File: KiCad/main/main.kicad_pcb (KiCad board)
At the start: 4 copper layers, 160 x 100.1 mm, 35 parts, among them SW1 SW_Push, U1 74HC245, U10 8254, U11 8259, U12 27C512, U2 8284, U3 74HC245, U4 8086, U5 74HC573, U6 74HC573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

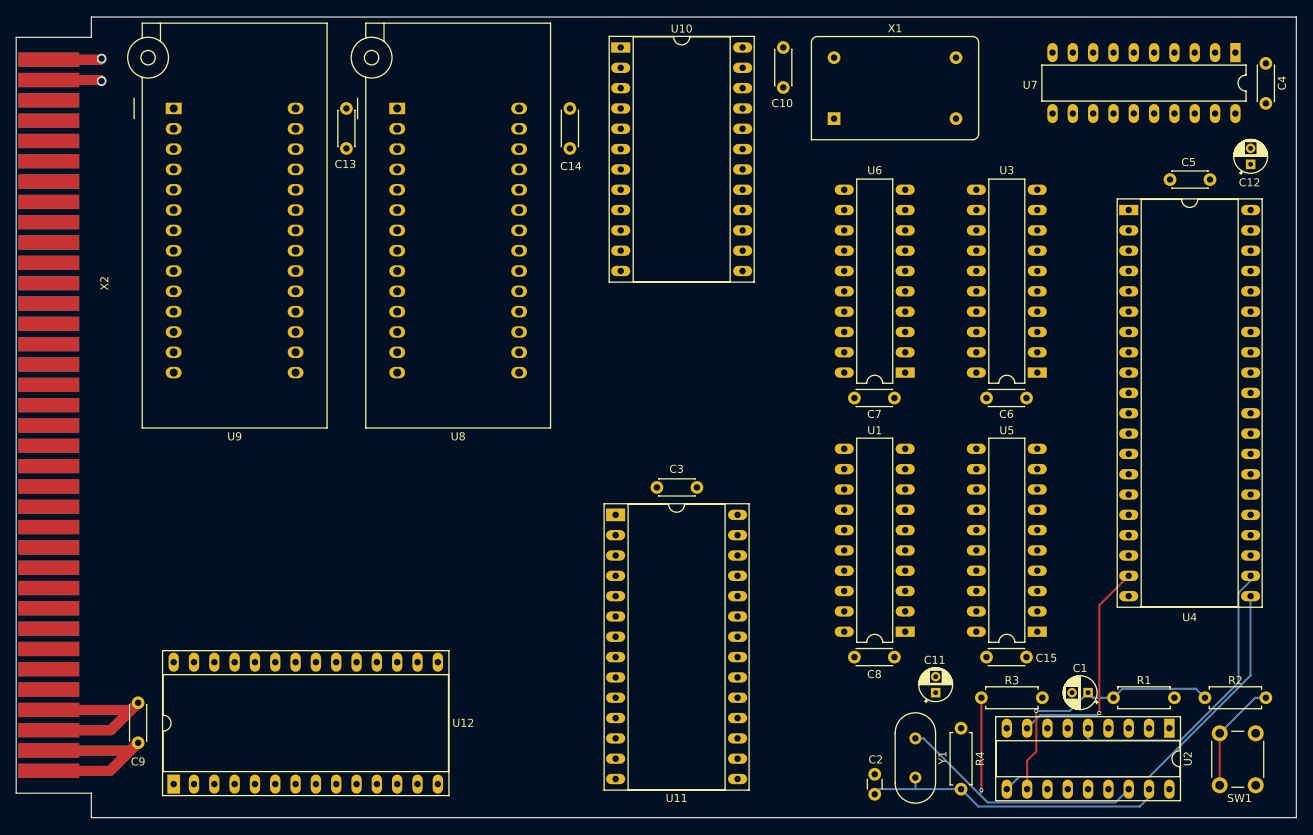
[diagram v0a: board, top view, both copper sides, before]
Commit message: Updated graphics adapter and main schematics + board.
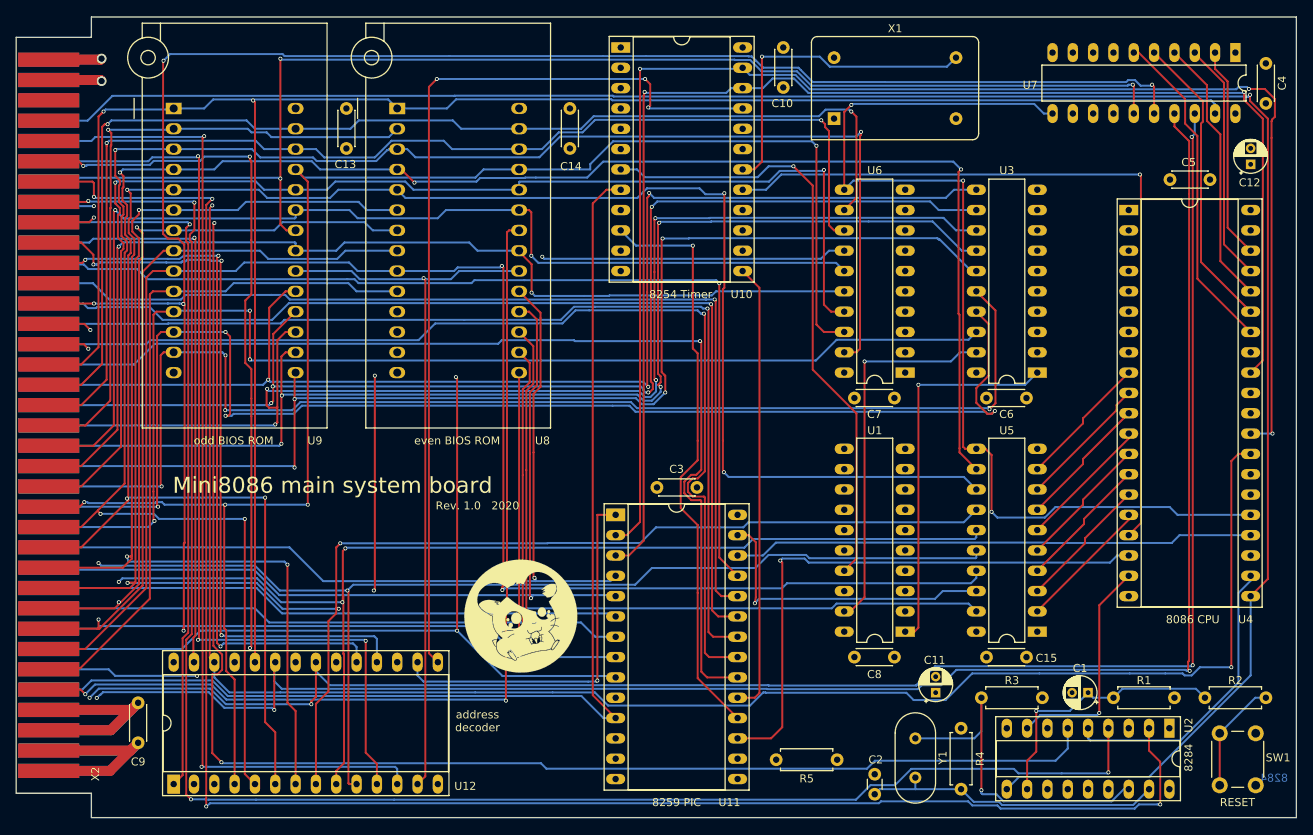
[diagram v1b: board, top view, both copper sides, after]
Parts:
- added G***: LOGO, Mini8086:hamtaro, F.Cu at (125.0, 112.3)
- added R5: 4K7, Resistor_THT:R_Axial_DIN0207_L6.3mm_D2.5mm_P7.62mm_Horizontal, F.Cu at (164.8, 130.3)
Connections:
- U11 pad 16: VCC -> Net-(R5-Pad2)
- U12 pad 17: ~IO2 -> ~IO_DBG
- X2 pad 31: Net-(X2-Pad31) -> ~IO_DBG
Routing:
- net ~WR: track 0.00 -> 356.7 mm, vias 0 -> 4
- net ~RD: track 0.00 -> 308.9 mm, vias 0 -> 3
- net A18: track 0.00 -> 270.2 mm, vias 0 -> 4
- net A17: track 0.00 -> 265.2 mm, vias 0 -> 5
- net A7: track 0.00 -> 255.2 mm, vias 0 -> 5
- net A6: track 0.00 -> 251.1 mm, vias 0 -> 5
- net A16: track 0.00 -> 249.1 mm, vias 0 -> 2
- net M_~IO: track 0.00 -> 240.7 mm, vias 0 -> 3
- net A19: track 0.00 -> 240.1 mm, vias 0 -> 5
- net A4: track 0.00 -> 234.6 mm, vias 0 -> 5
- net A3: track 0.00 -> 234.5 mm, vias 0 -> 3
- net A5: track 0.00 -> 233.4 mm, vias 0 -> 4
- net A8: track 0.00 -> 232.6 mm, vias 0 -> 4
- net PCLK: track 0.00 -> 228.8 mm, vias 0 -> 4
- net RESET: track 46.3 -> 262.4 mm, vias 0 -> 1
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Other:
- board text added: "8086 CPU"
- board text added: "8254 Timer"
- board text added: "8259 PIC"
- board text added: "8284"
- board text added: "Mini8086 main system board"
- board text added: "RESET"
- board text added: "Rev. 1.0 2020"
- board text added: "address decoder"
- board text added: "even BIOS ROM"
- board text added: "odd BIOS ROM"

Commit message: Updated KiCad VGA board and main board.
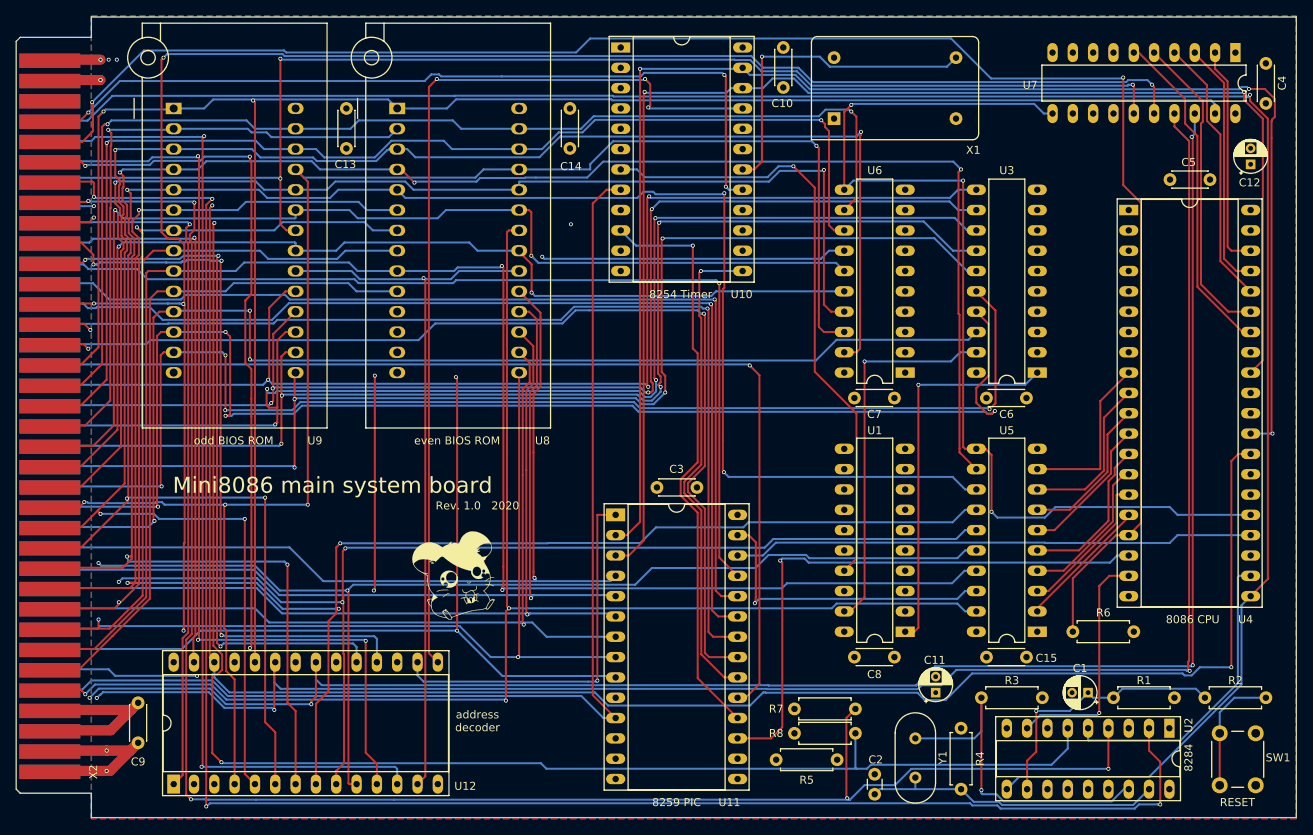
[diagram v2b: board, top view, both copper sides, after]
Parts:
- added R6: 4K7, Resistor_THT:R_Axial_DIN0207_L6.3mm_D2.5mm_P7.62mm_Horizontal, F.Cu at (194.3, 114.3)
- added R7: 4K7, Resistor_THT:R_Axial_DIN0207_L6.3mm_D2.5mm_P7.62mm_Horizontal, F.Cu at (159.5, 124.0)
- added R8: 4K7, Resistor_THT:R_Axial_DIN0207_L6.3mm_D2.5mm_P7.62mm_Horizontal, F.Cu at (159.5, 127.0)
- X2: value Edge72-Mini8086 -> Edge72
- moved G*** 8.53 mm to (118.1, 107.2)
- moved X2 0.18 mm to (66.4, 131.8)
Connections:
- net Net-(U10-Pad10) renamed /PIC TIMER/IRQ0
- net ~IO0 renamed ~IO_TIMER
- net ~IO1 renamed ~IO_PIC
- U10 pad 13: Net-(U10-Pad13) -> /PIC TIMER/IRQ2
- U10 pad 17: NMI -> TMR2
- U11 pad 19: Net-(U10-Pad13) -> IRQ1
- U11 pad 20: IRQ2 -> /PIC TIMER/IRQ2
- U2 pad 15: GND -> Net-(U2-Pad15)
- X2 pad 32: Net-(X2-Pad32) -> NMI
- X2 pad 33: Net-(X2-Pad33) -> TMR2
- X2 pad 57: IRQ2 -> IRQ1
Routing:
- net IRQ2: track 131.8 -> 0.00 mm, vias 1 -> 0
- net IRQ1: track 0.00 -> 131.4 mm, vias 0 -> 1
- net NMI: track 96.2 -> 218.8 mm, vias 1 -> 2
- net TMR2: track 0.00 -> 104.0 mm, vias 0 -> 3
- net /PIC TIMER/IRQ2: track 0.00 -> 60.8 mm, vias 0 -> 1
- net Net-(U10-Pad13): track 56.6 -> 0.00 mm
- net RDY2: track 215.9 -> 227.3 mm, vias 4 -> 5
- net AD7: track 34.1 -> 38.7 mm
- net RDY1: track 200.2 -> 204.7 mm
- net ~DEN: track 92.7 -> 88.8 mm
- net AD6: track 34.1 -> 37.6 mm
- net AD3: track 34.1 -> 37.2 mm
- net AD5: track 34.1 -> 36.5 mm
- net AD2: track 34.1 -> 36.4 mm
- net ~RD: track 308.9 -> 306.7 mm
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- added copper zone on B.Cu, net GND
- added copper zone on F.Cu, net GND
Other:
- outline, holes or cut-outs redrawn

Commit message: Updated main system board schematics and board.
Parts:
- added C16: 100n, Capacitor_THT:C_Disc_D4.3mm_W1.9mm_P5.00mm, F.Cu at (118.7, 119.1)
- added C17: 100n, Capacitor_THT:C_Disc_D4.3mm_W1.9mm_P5.00mm, F.Cu at (156.0, 75.2)
- added R10: 10K, Resistor_THT:R_Axial_DIN0207_L6.3mm_D2.5mm_P2.54mm_Vertical, F.Cu at (159.5, 116.7)
- added R11: 10K, Resistor_THT:R_Axial_DIN0207_L6.3mm_D2.5mm_P2.54mm_Vertical, F.Cu at (159.5, 112.9)
- added R12: 10K, Resistor_THT:R_Axial_DIN0207_L6.3mm_D2.5mm_P2.54mm_Vertical, F.Cu at (159.5, 109.1)
- added R13: 10K, Resistor_THT:R_Axial_DIN0207_L6.3mm_D2.5mm_P2.54mm_Vertical, F.Cu at (159.5, 105.3)
- added R14: 10K, Resistor_THT:R_Axial_DIN0207_L6.3mm_D2.5mm_P2.54mm_Vertical, F.Cu at (159.5, 101.5)
- added R9: 10K, Resistor_THT:R_Axial_DIN0207_L6.3mm_D2.5mm_P2.54mm_Vertical, F.Cu at (159.5, 120.5)
- added U13: 74HC32, Package_DIP:DIP-14_W7.62mm_LongPads, F.Cu at (145.2, 75.2)
- added U14: 74HC245, Package_SO:SO-20_12.8x7.5mm_P1.27mm, F.Cu at (126.5, 127.5)
- added U15: 74HC08, Package_DIP:DIP-14_W7.62mm_LongPads, F.Cu at (109.7, 95.5)
- C11: value 10µ -> 100µ; footprint Capacitor_THT:CP_Radial_D4.0mm_P2.00mm -> Capacitor_THT:CP_Radial_D8.0mm_P3.50mm
- C12: value 10µ -> 47µ
- R7, R8: value 4K7 -> 10K
- moved C11 80.2 mm to (101.6, 95.0), turned to 270 degrees
- moved G*** 10.1 mm to (127.4, 103.3)
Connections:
- net Net-(C1-Pad1) renamed /CPU/~RES
- net Net-(U2-Pad5) renamed /CPU/READY
- net Net-(U2-Pad8) renamed /CPU/CLK
- net Net-(U4-Pad25) renamed /CPU/ALE
- U1 pad 19: ~DEN -> /CPU/~CE_DLO
- U10 pad 19: A1 -> A0
- U10 pad 20: A2 -> A1
- U11 pad 27: A1 -> A0
- U12 pad 3: GND -> A10
- U2 pad 10: RESET -> /CPU/CPU_RESET
- U3 pad 19: ~DEN -> /CPU/~CE_DHI
- U4 pad 21: RESET -> /CPU/CPU_RESET
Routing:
- net RESET: track 262.4 -> 105.4 mm
- net /CPU/CPU_RESET: track 0.00 -> 154.2 mm, vias 0 -> 1
- net A0: track 178.2 -> 304.8 mm, vias 3 -> 5
- net A2: track 286.0 -> 201.3 mm
- net VCC: track 607.6 -> 673.2 mm, vias 0 -> 5
- net Net-(U13-Pad10): track 0.00 -> 64.4 mm, vias 0 -> 1
- net /glue logic/~CE_HI2LO: track 0.00 -> 59.3 mm, vias 0 -> 2
- net A10: track 156.1 -> 209.9 mm, vias 2 -> 4
- net ~INTA: track 65.2 -> 117.9 mm, vias 0 -> 1
- net D15: track 154.1 -> 205.8 mm, vias 3 -> 4
- net M_~IO: track 240.7 -> 292.3 mm, vias 3 -> 5
- net D14: track 152.8 -> 201.2 mm
- net D8: track 149.8 -> 197.3 mm, vias 3 -> 4
- net D12: track 153.3 -> 199.2 mm, vias 4 -> 5
- net D11: track 150.5 -> 195.1 mm, vias 4 -> 5
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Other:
- board text added: "1 MHz"
- board text added: "8254 PIT"
- board text removed: "8254 Timer"

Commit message: Fixed main and info_board bugs.
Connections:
- R7 pad 1: GND -> VCC
- R8 pad 1: GND -> VCC
- U4 pad 31: Net-(U4-Pad31) -> GND
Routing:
- net VCC: track 673.2 -> 682.9 mm
- net GND: vias 18 -> 32
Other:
- board text added: "Rev. 1.1 2020"
- board text removed: "Rev. 1.0 2020"

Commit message: Replaced MAX7000 CPLD with MAX II in graphics adapter. PCB redesign with smaller size.
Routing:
- net GND: vias 32 -> 48

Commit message: Fixed CPU board bugs.
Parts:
- R10, R11, R12, R13, R14, R9: value 10K -> 3K3
- R7, R8: value 10K -> 4K7
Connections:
- R7 pad 1: VCC -> GND
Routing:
- net VCC: track 682.9 -> 678.2 mm
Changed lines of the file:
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@@
   (page A4)
   (layers
-    (0 F.Cu signal)
-    (1 In1.Cu signal)
+    (0 F.Cu signal hide)
+    (1 In1.Cu signal hide)
     (2 In2.Cu power hide)
-    (31 B.Cu signal)
+    (31 B.Cu signal hide)
     (32 B.Adhes user hide)
     (33 F.Adhes user hide)
@@
       (effects (font (size 1 1) (thickness 0.15)))
     )
-    (fp_text value 10K (at 1.27 2.37) (layer F.Fab)
+    (fp_text value 3K3 (at 1.27 2.37) (layer F.Fab)
       (effects (font (size 1 1) (thickness 0.15)))
     )
@@
       (effects (font (size 1 1) (thickness 0.15)))
     )
-    (fp_text value 10K (at 1.27 2.37) (layer F.Fab)
+    (fp_text value 3K3 (at 1.27 2.37) (layer F.Fab)
       (effects (font (size 1 1) (thickness 0.15)))
     )
@@
       (effects (font (size 1 1) (thickness 0.15)))
     )
-    (fp_text value 10K (at 1.27 2.37) (layer F.Fab)
+    (fp_text value 3K3 (at 1.27 2.37) (layer F.Fab)
       (effects (font (size 1 1) (thickness 0.15)))
     )
@@
       (effects (font (size 1 1) (thickness 0.15)))
     )
-    (fp_text value 10K (at 1.27 2.37) (layer F.Fab)
+    (fp_text value 3K3 (at 1.27 2.37) (layer F.Fab)
       (effects (font (size 1 1) (thickness 0.15)))
     )
@@
       (effects (font (size 1 1) (thickness 0.15)))
     )
-    (fp_text value 10K (at 1.27 2.37) (layer F.Fab)
+    (fp_text value 3K3 (at 1.27 2.37) (layer F.Fab)
       (effects (font (size 1 1) (thickness 0.15)))
     )
@@
       (effects (font (size 1 1) (thickness 0.15)))
     )
-    (fp_text value 10K (at 1.27 2.37) (layer F.Fab)
+    (fp_text value 3K3 (at 1.27 2.37) (layer F.Fab)
       (effects (font (size 1 1) (thickness 0.15)))
     )
@@
       (effects (font (size 1 1) (thickness 0.15)))
     )
-    (fp_text value 10K (at 3.81 2.37) (layer F.Fab)
+    (fp_text value 4K7 (at 3.81 2.37) (layer F.Fab)
       (effects (font (size 1 1) (thickness 0.15)))
     )
@@
       (effects (font (size 1 1) (thickness 0.15)))
     )
-    (fp_text value 10K (at 3.81 2.37) (layer F.Fab)
+    (fp_text value 4K7 (at 3.81 2.37) (layer F.Fab)
       (effects (font (size 1 1) (thickness 0.15)))
     )
@@
       (net 25 RDY2))
     (pad 1 thru_hole circle (at 0 0) (size 1.6 1.6) (drill 0.8) (layers *.Cu *.Mask)
-      (net 2 VCC))
+      (net 1 GND))
     (model ${KISYS3DMOD}/Resistor_THT.3dshapes/R_Axial_DIN0207_L6.3mm_D2.5mm_P7.62mm_Horizontal.wrl
       (at (xyz 0 0 0))
@@
   (segment (start 152.4 95.758) (end 152.4 92.456) (width 1.25) (layer In1.Cu) (net 2))
   (segment (start 206.375 122.555) (end 207.01 122.555) (width 1.75) (layer In1.Cu) (net 2))
-  (segment (start 196.596 88.138) (end 196.596 112.776) (width 1.75) (layer In1.Cu) (net 2))
   (segment (start 208.534 124.079) (end 207.01 122.555) (width 1.25) (layer In1.Cu) (net 2))
   (segment (start 206.375 133.985) (end 208.534 131.826) (width 1.25) (layer In1.Cu) (net 2))
@@
   (segment (start 169.545 132.12) (end 169.545 130.429) (width 1.25) (layer In1.Cu) (net 2))
   (segment (start 169.545 130.429) (end 169.545 120.015) (width 1.25) (layer In1.Cu) (net 2))
-  (segment (start 196.596 112.776) (end 203.327 119.507) (width 1.75) (layer In1.Cu) (net 2))
   (segment (start 202.920001 119.100001) (end 203.327 119.507) (width 1.25) (layer In1.Cu) (net 2))
   (segment (start 203.327 119.507) (end 206.375 122.555) (width 1.75) (layer In1.Cu) (net 2))
@@
   (segment (start 182.245 87.503) (end 182.88 88.138) (width 1.25) (layer In1.Cu) (net 2))
   (segment (start 166.116 88.138) (end 182.88 88.138) (width 1.75) (layer In1.Cu) (net 2))
-  (segment (start 182.88 88.138) (end 196.596 88.138) (width 1.75) (layer In1.Cu) (net 2))
   (segment (start 182.372 85.09) (end 182.245 85.217) (width 1.25) (layer In1.Cu) (net 2))
   (segment (start 183.515 85.09) (end 182.372 85.09) (width 1.25) (layer In1.Cu) (net 2))
@@
   (segment (start 162.814 130.302) (end 159.512 127) (width 0.4) (layer In1.Cu) (net 2))
   (segment (start 164.846 130.302) (end 162.814 130.302) (width 0.4) (layer In1.Cu) (net 2))
-  (segment (start 159.512 127) (end 159.512 123.952) (width 0.4) (layer In1.Cu) (net 2))
+  (segment (start 196.596 112.776) (end 203.327 119.507) (width 1.75) (layer In1.Cu) (net 2))
+  (segment (start 196.596 90.932) (end 196.596 112.776) (width 1.75) (layer In1.Cu) (net 2))
+  (segment (start 182.88 88.138) (end 193.802 88.138) (width 1.75) (layer In1.Cu) (net 2))
+  (segment (start 193.802 88.138) (end 196.596 90.932) (width 1.75) (layer In1.Cu) (net 2))
   (segment (start 170.18 133.985) (end 169.545 134.62) (width 0.25) (layer B.Cu) (net 3))
   (segment (start 174.625 132.535) (end 174.625 133.985) (width 0.25) (layer B.Cu) (net 3))
